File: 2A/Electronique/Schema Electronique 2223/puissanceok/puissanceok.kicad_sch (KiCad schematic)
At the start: 17 parts, among them J101 Bat 2, J102 Bat 1, J103 AU, J104 Switch, J113 Conn_02x20_Odd_Even

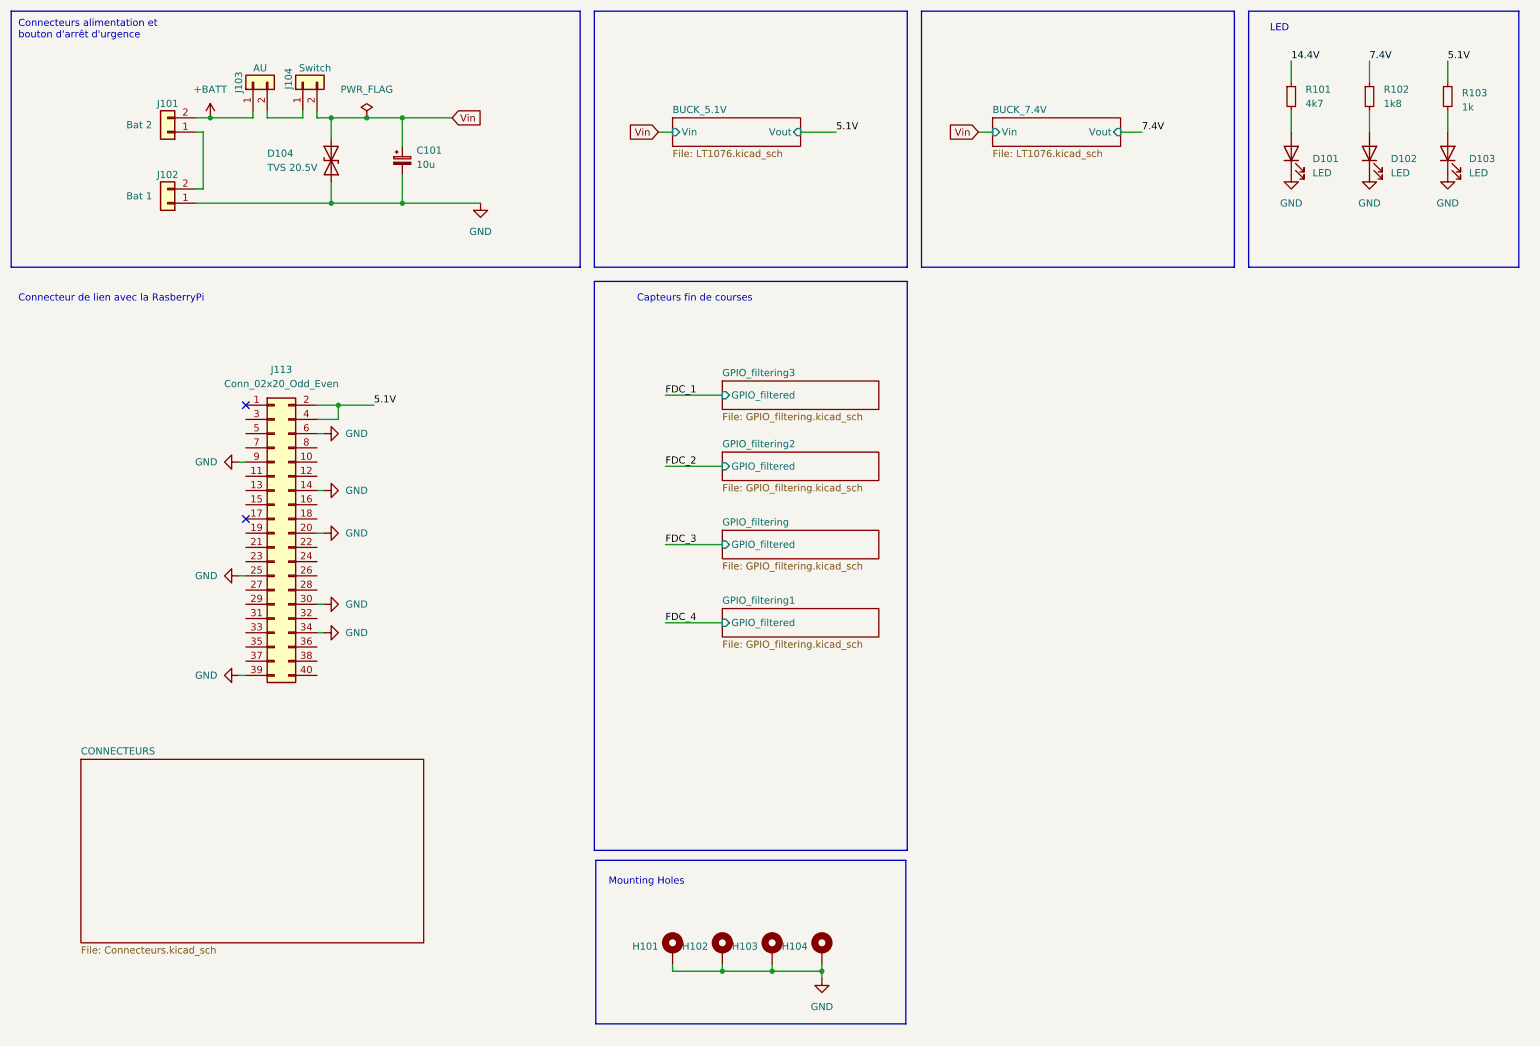
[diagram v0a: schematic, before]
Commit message: update schematic
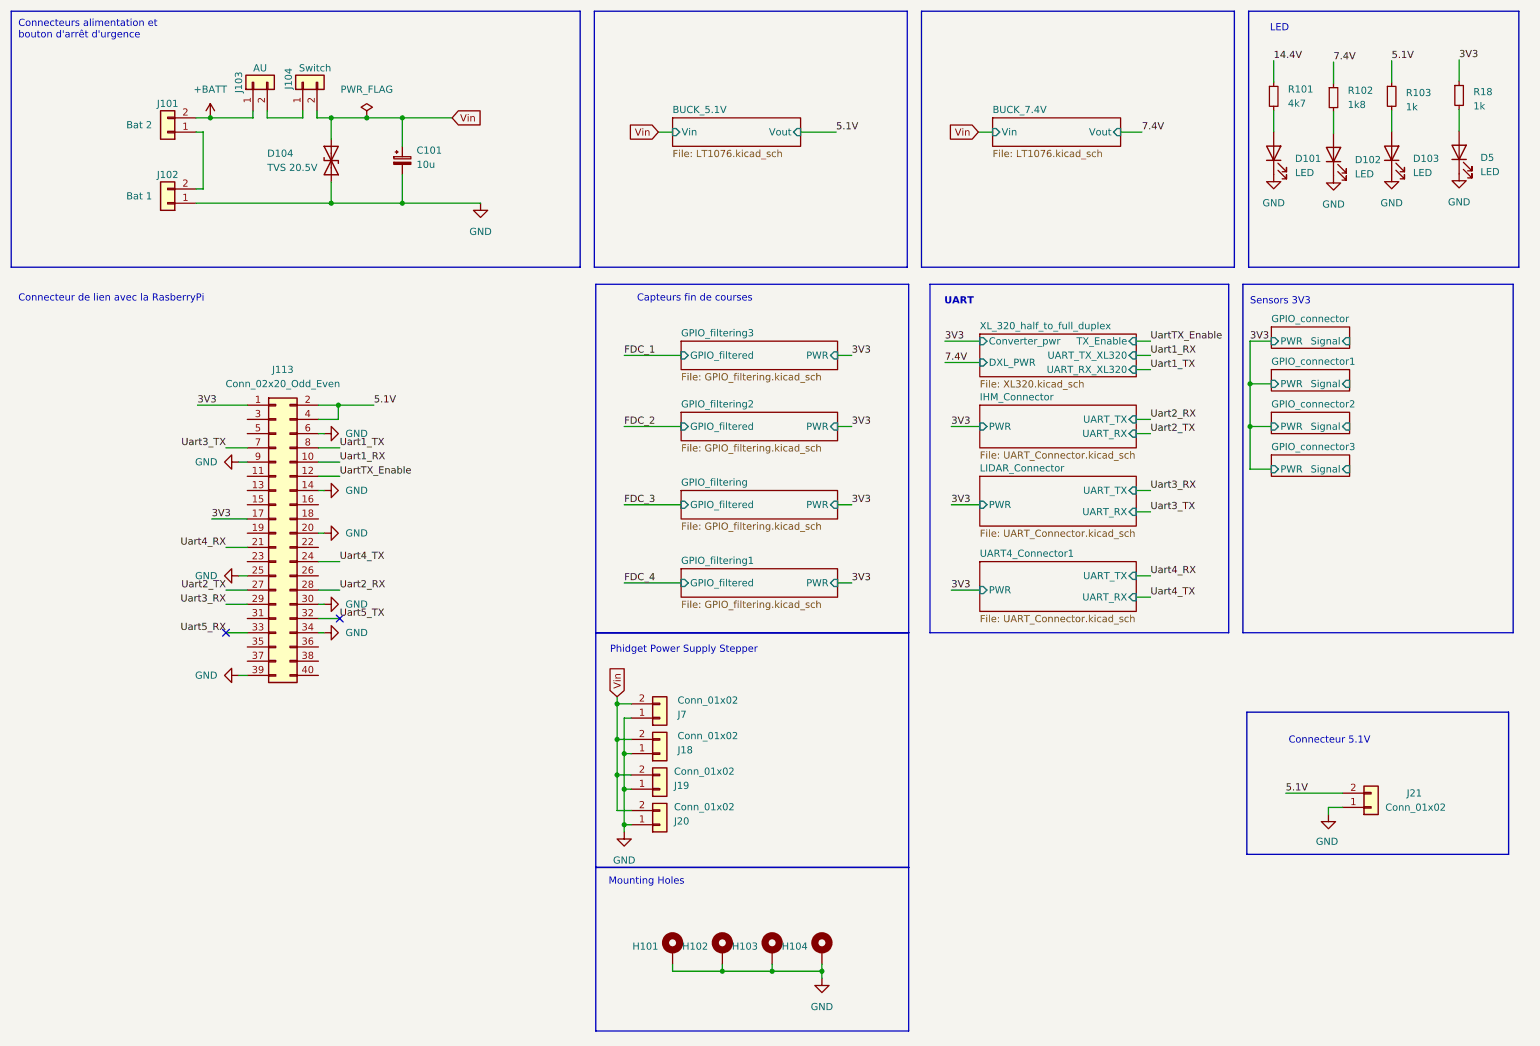
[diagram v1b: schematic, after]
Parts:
- added D5: LED, LED_SMD:LED_0603_1608Metric_Pad1.05x0.95mm_HandSolder, symbol Device:LED
- added J18, J19, J20, J21, J7: Conn_01x02, symbol Connector_Generic:Conn_01x02
- added R18: 1k, Resistor_SMD:R_0603_1608Metric_Pad0.98x0.95mm_HandSolder, symbol Device:R_Small
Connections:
- net 5.1V: now also J21.2 (Pin_2)
- net GND: now also D5.1 (K), J18.1 (Pin_1), J19.1 (Pin_1), J20.1 (Pin_1), J21.1 (Pin_1), J7.1 (Pin_1)
- net Vin: now also J18.2 (Pin_2), J19.2 (Pin_2), J20.2 (Pin_2), J7.2 (Pin_2)
- net 3V3: now reaches J113.1 (Pin_1)
- net 3V3: now also J113.17 (Pin_17), R18.1
- net Uart1_RX: now reaches J113.10 (Pin_10)
- net UartTX_Enable: now reaches J113.12 (Pin_12)
- net Uart4_RX: now reaches J113.21 (Pin_21)
- net Uart4_TX: now reaches J113.24 (Pin_24)
- net Uart2_TX: now reaches J113.27 (Pin_27)
- net Uart2_RX: now reaches J113.28 (Pin_28)
- net Uart3_RX: now reaches J113.29 (Pin_29)
- net Uart5_TX: now reaches J113.32 (Pin_32)
- net Uart5_RX: now reaches J113.33 (Pin_33)
- net Uart3_TX: now reaches J113.7 (Pin_7)
- net Uart1_TX: now reaches J113.8 (Pin_8)
- new net: D5.2 (A), R18.2
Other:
- removed sheet CONNECTEURS
- added sheet GPIO_connector (gpioconnector.kicad_sch)
- added sheet GPIO_connector1 (gpioconnector.kicad_sch)
- added sheet GPIO_connector2 (gpioconnector.kicad_sch)
- added sheet GPIO_connector3 (gpioconnector.kicad_sch)
- added sheet IHM_Connector (UART_Connector.kicad_sch)
- added sheet LIDAR_Connector (UART_Connector.kicad_sch)
- added sheet UART4_Connector1 (UART_Connector.kicad_sch)
- added sheet XL_320_half_to_full_duplex (XL320.kicad_sch)
- sheet GPIO_filtering ports: added PWR; removed none
- sheet GPIO_filtering1 ports: added PWR; removed none
- sheet GPIO_filtering2 ports: added PWR; removed none
- sheet GPIO_filtering3 ports: added PWR; removed none
- note added: "Connecteur 5.1V"
- note added: "Phidget Power Supply Stepper"
- note added: "Sensors 3V3"
- note added: "UART"
- moved on the sheet: D101, D102, D103, R101, R102, R103

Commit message: update schematic
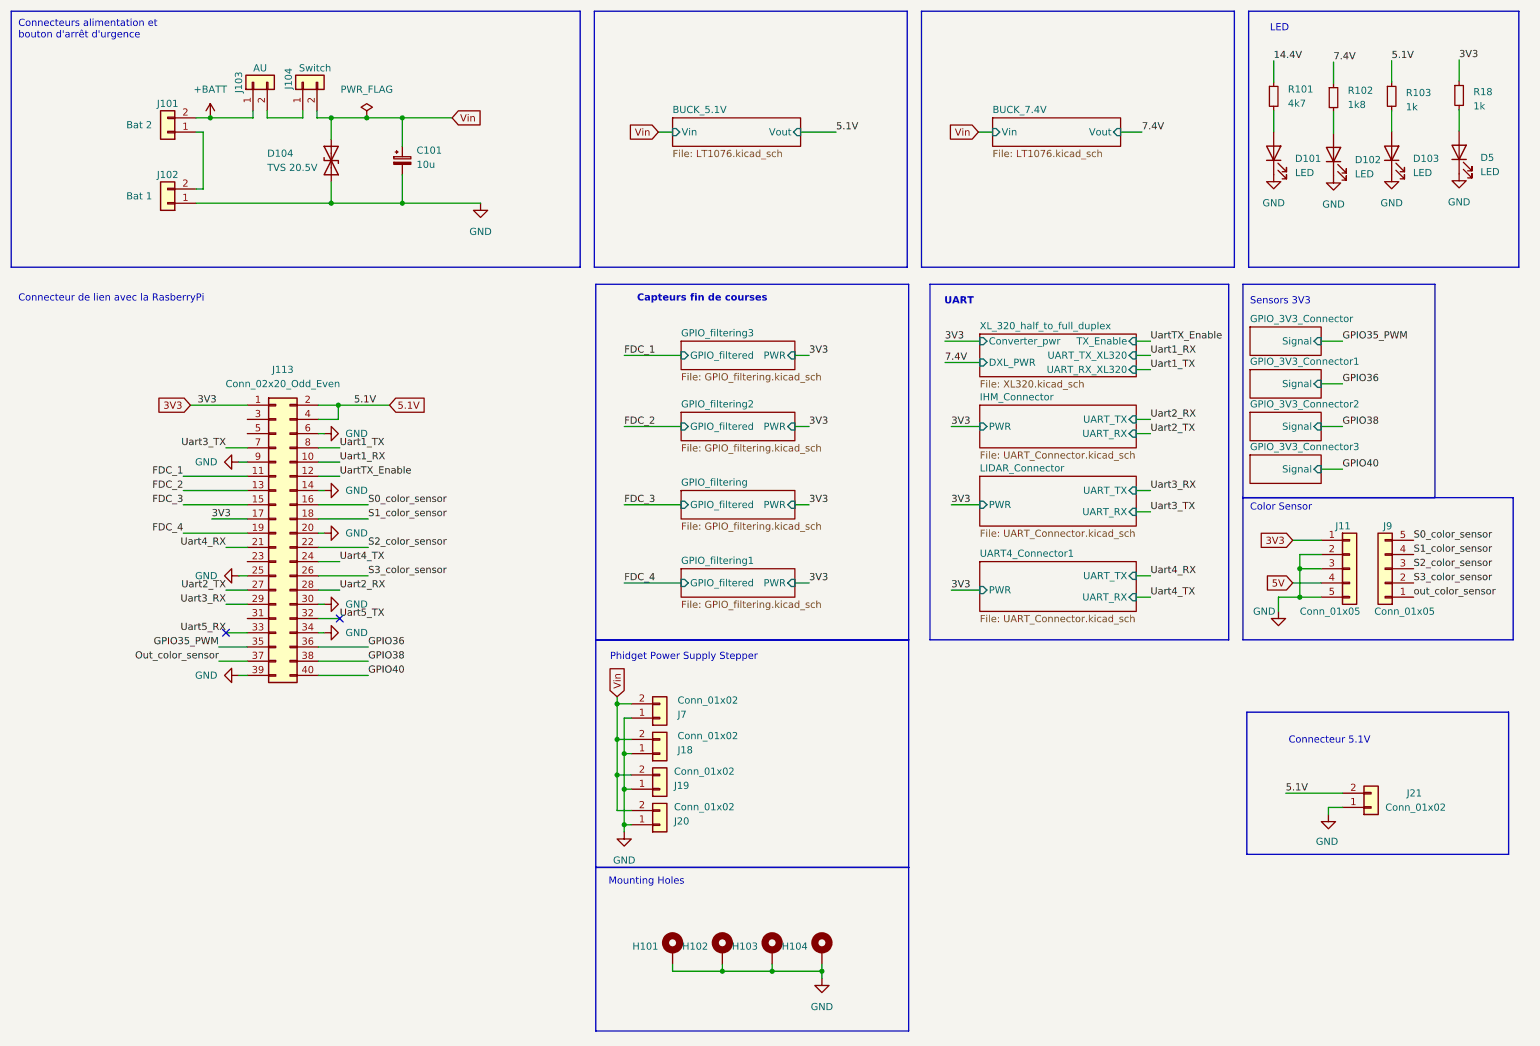
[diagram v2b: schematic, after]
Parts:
- added J11, J9: Conn_01x05, symbol Connector_Generic:Conn_01x05
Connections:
- net 3V3: now also J11.1 (Pin_1)
- net FDC_1: now also J113.11 (Pin_11)
- net FDC_2: now also J113.13 (Pin_13)
- net FDC_3: now also J113.15 (Pin_15)
- net FDC_4: now also J113.19 (Pin_19)
- net GND: now also J11.2 (Pin_2), J11.3 (Pin_3), J11.5 (Pin_5)
- net S0_color_sensor: now reaches J113.16 (Pin_16)
- net S0_color_sensor: now also J9.5 (Pin_5)
- net S1_color_sensor: now reaches J113.18 (Pin_18)
- net S1_color_sensor: now also J9.4 (Pin_4)
- net S2_color_sensor: now reaches J113.22 (Pin_22)
- net S2_color_sensor: now also J9.3 (Pin_3)
- net S3_color_sensor: now reaches J113.26 (Pin_26)
- net S3_color_sensor: now also J9.2 (Pin_2)
- net GPIO35_PWM: now reaches J113.35 (Pin_35)
- net GPIO36: now reaches J113.36 (Pin_36)
- net Out_color_sensor: now reaches J113.37 (Pin_37)
- net GPIO38: now reaches J113.38 (Pin_38)
- net GPIO40: now reaches J113.40 (Pin_40)
- new net 5V: J11.4 (Pin_4)
- new net out_color_sensor: J9.1 (Pin_1)
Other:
- removed sheet GPIO_connector
- removed sheet GPIO_connector1
- removed sheet GPIO_connector2
- removed sheet GPIO_connector3
- added sheet GPIO_3V3_Connector (GPIO_3V3_Connector.kicad_sch)
- added sheet GPIO_3V3_Connector1 (GPIO_3V3_Connector.kicad_sch)
- added sheet GPIO_3V3_Connector2 (GPIO_3V3_Connector.kicad_sch)
- added sheet GPIO_3V3_Connector3 (GPIO_3V3_Connector.kicad_sch)
- note added: "Color Sensor"

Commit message: pcb puissance update
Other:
- sheet XL_320_half_to_full_duplex renamed XL_320_connector_and_buffer
- moved on the sheet: H101, H102, H103, H104, J11, J21, J9
